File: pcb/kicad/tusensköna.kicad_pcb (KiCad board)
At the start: 2 copper layers, 93.2 x 50.5 mm, 29 parts, among them J1 AudioJack3, J2 AudioJack3, J3 Micro_SD_Card, J4 Conn_01x12_Pin, SW1 SW_Push, SW2 SW_Push, U1 Electrosmith_Daisy_Seed_Rev4

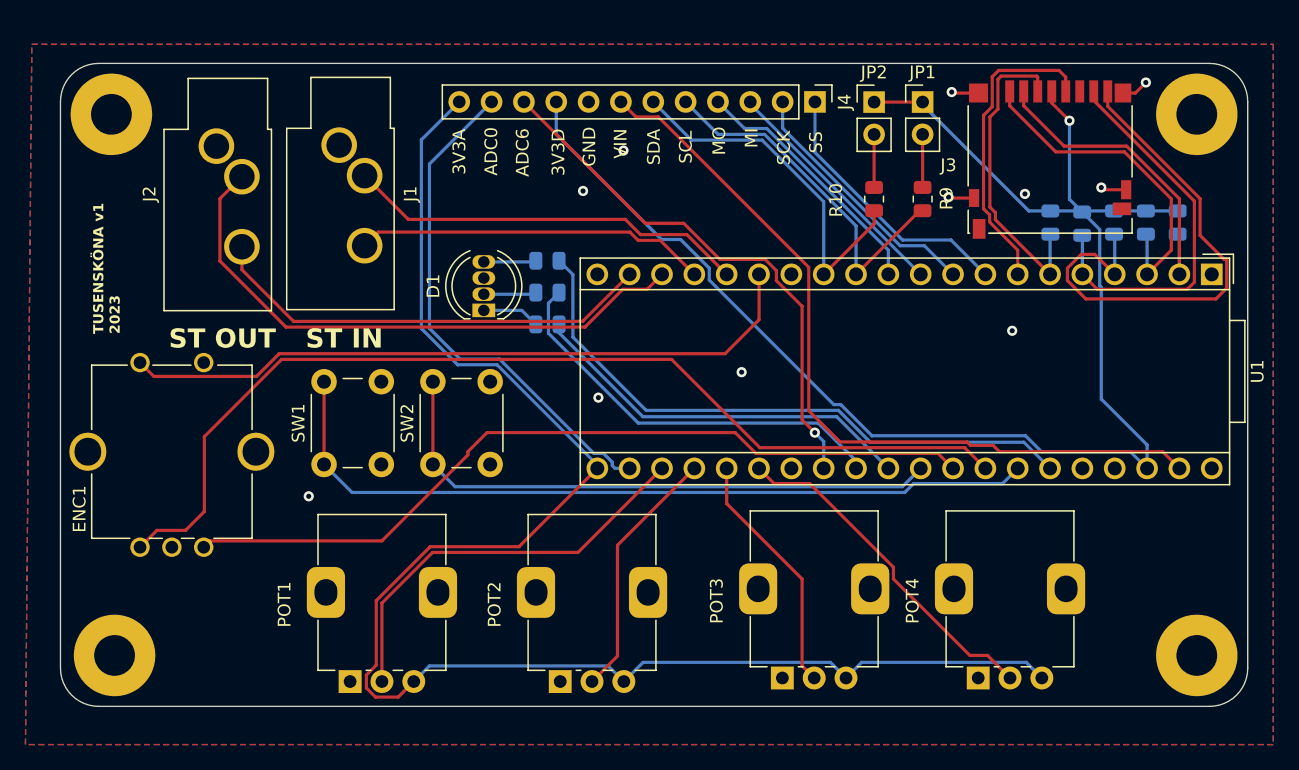
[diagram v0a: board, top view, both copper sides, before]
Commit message: fixed ground plane
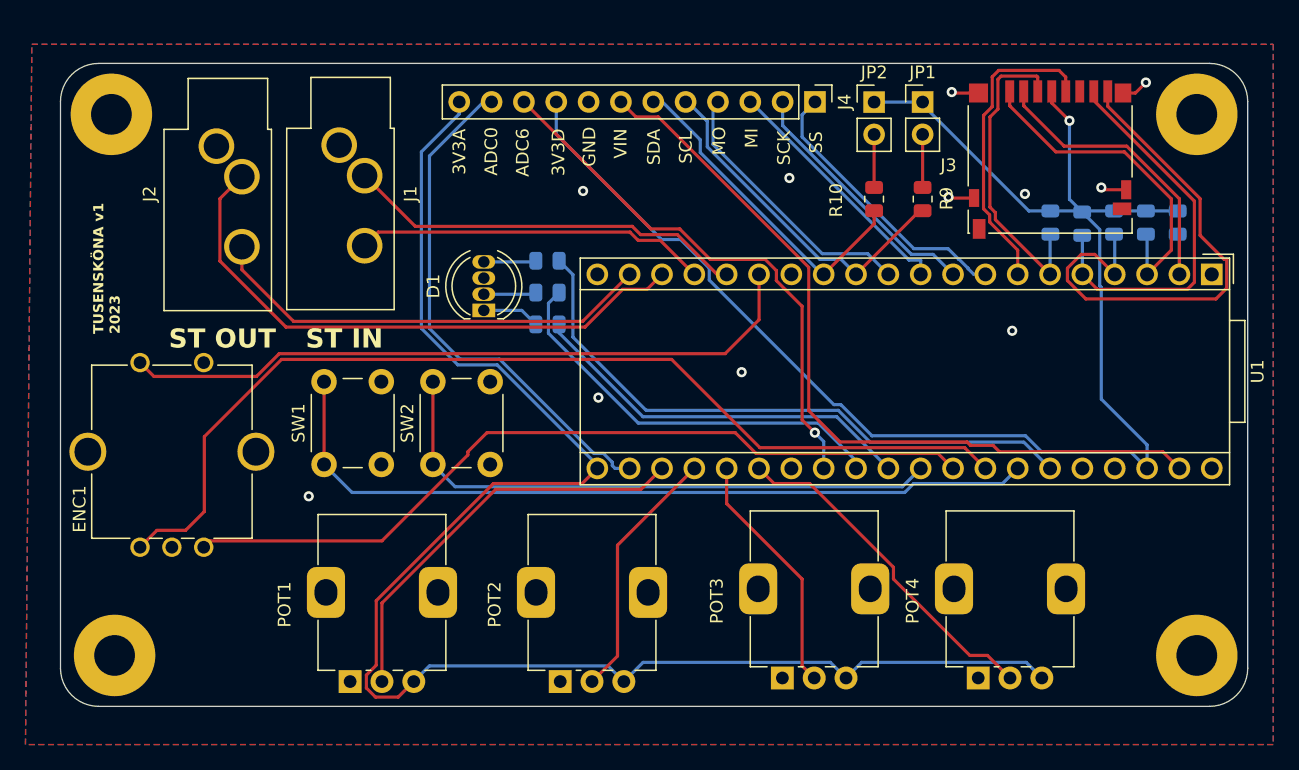
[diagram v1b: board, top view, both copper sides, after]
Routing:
- net /SDA: track 29.1 -> 26.4 mm
- net /SPI_PICO: track 20.3 -> 21.7 mm
- net /SCL: track 28.5 -> 27.5 mm
- net /SPI_CS: track 21.3 -> 22.1 mm
- net /SPI_POCI: track 19.1 -> 19.7 mm

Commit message: schematic and gnd plane
Fixed errors where connection to gnd plane was insufficient for some components.
Moved some components to make space for heat dissipation.
Cleaned up part of schematic regarding pullup resistors.
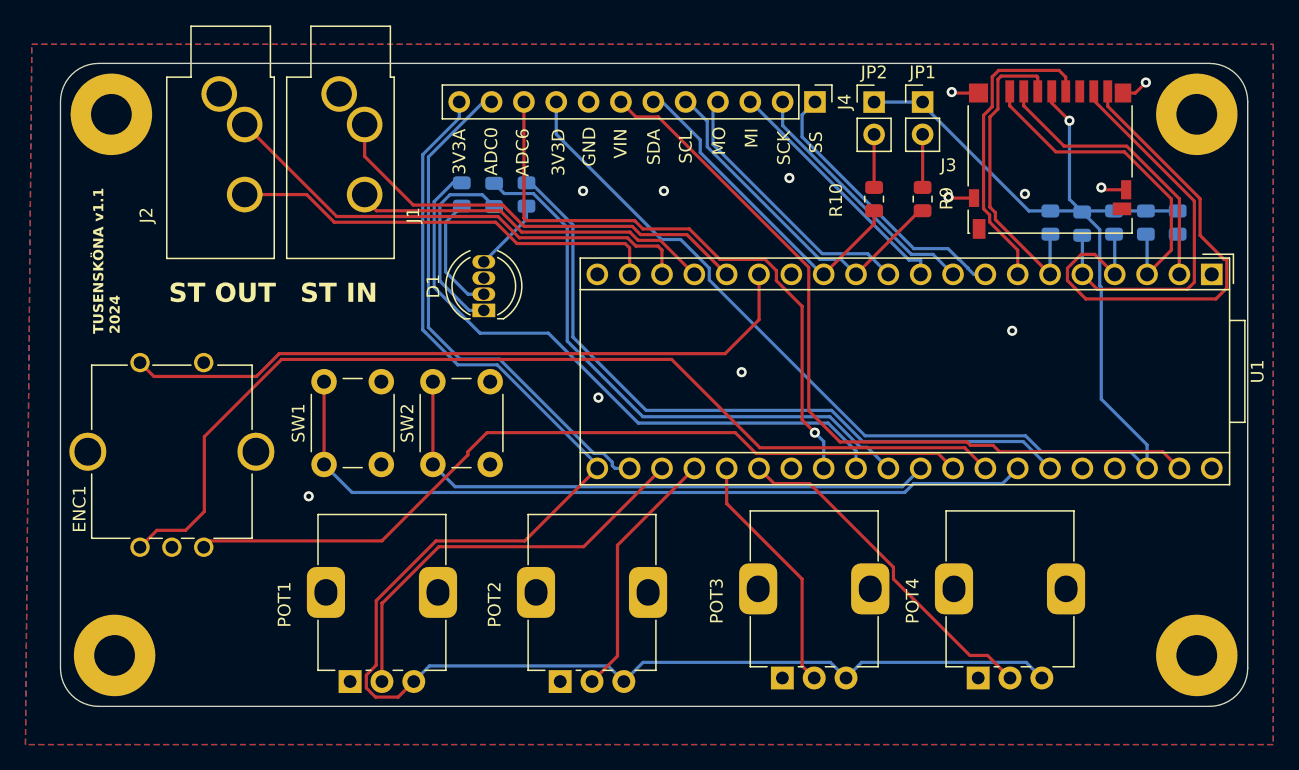
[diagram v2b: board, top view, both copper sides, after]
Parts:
- moved R7 11.0 mm to (130.8, 33.3), turned to -90 degrees
- moved R6 10.2 mm to (128.3, 33.3), turned to -90 degrees
- moved R8 5.46 mm to (133.3, 33.3), turned to -90 degrees
- moved J2 4.11 mm to (109.2, 25.4)
- moved J1 4.02 mm to (118.6, 25.4)
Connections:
- net /SCL renamed /I2C_SCL
- net /SDA renamed /I2C_SDA
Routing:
- net /LED 1: track 32.4 -> 49.4 mm
- net /LED 2: track 30.9 -> 45.5 mm
- net Net-(D1-GA): track 4.54 -> 15.4 mm
- net /LED 3: track 48.2 -> 55.6 mm
- net /STEREO OUT L: track 45.9 -> 39.1 mm
- net /ADC6: track 42.4 -> 47.7 mm
- net Net-(D1-BA): track 4.14 -> 9.42 mm
- net /STEREO IN L: track 31.6 -> 35.5 mm
- net Net-(D1-RA): track 4.12 -> 5.77 mm
- net /STEREO OUT R: track 35.5 -> 34.0 mm
- net /STEREO IN R: track 27.7 -> 28.7 mm
- net /AGND: vias 11 -> 12
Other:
- board text added: "TUSENSKÖNA v1.1 2024"
- board text removed: "TUSENSKÖNA v1 2023"
